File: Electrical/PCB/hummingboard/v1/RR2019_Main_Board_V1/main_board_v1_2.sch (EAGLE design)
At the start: 144 parts, among them CN1 MIRCO_B, IC1 OR_SC70-5, J10 I2C_5V_4, J11 SERVO_LEFT, J12 SERVO_RIGHT, J13 ESC, J14 5V_INPUT, J15 QUAD_ENCODER_2, J16 7.2V_INPUT, J17 I2C_5V_FXIO_1, J18 I2C_5V_FXIO_2, J19 JETSON_TRIGGER, J2 REAR_ENCODER, J20 QUAD_ENCODER_1, J21 BLDC_HALL, J22 SPI_FXIO_1, J3 FRONT_ENCODER, J4 I2C_1V8_1, J5 SPI_2, J6 WIRELESS_MODULE, J7 UART_0, J8 UART_2, J9 STEERING_ANGLE, Q1 BSS138, Q3 DMP2066LSN, Q4 BSS138, Q5 BSS138, Q6 BSS138, Q7 BSS138, Q8 BSS138, U3 ICM-20948, U4 PCA9306

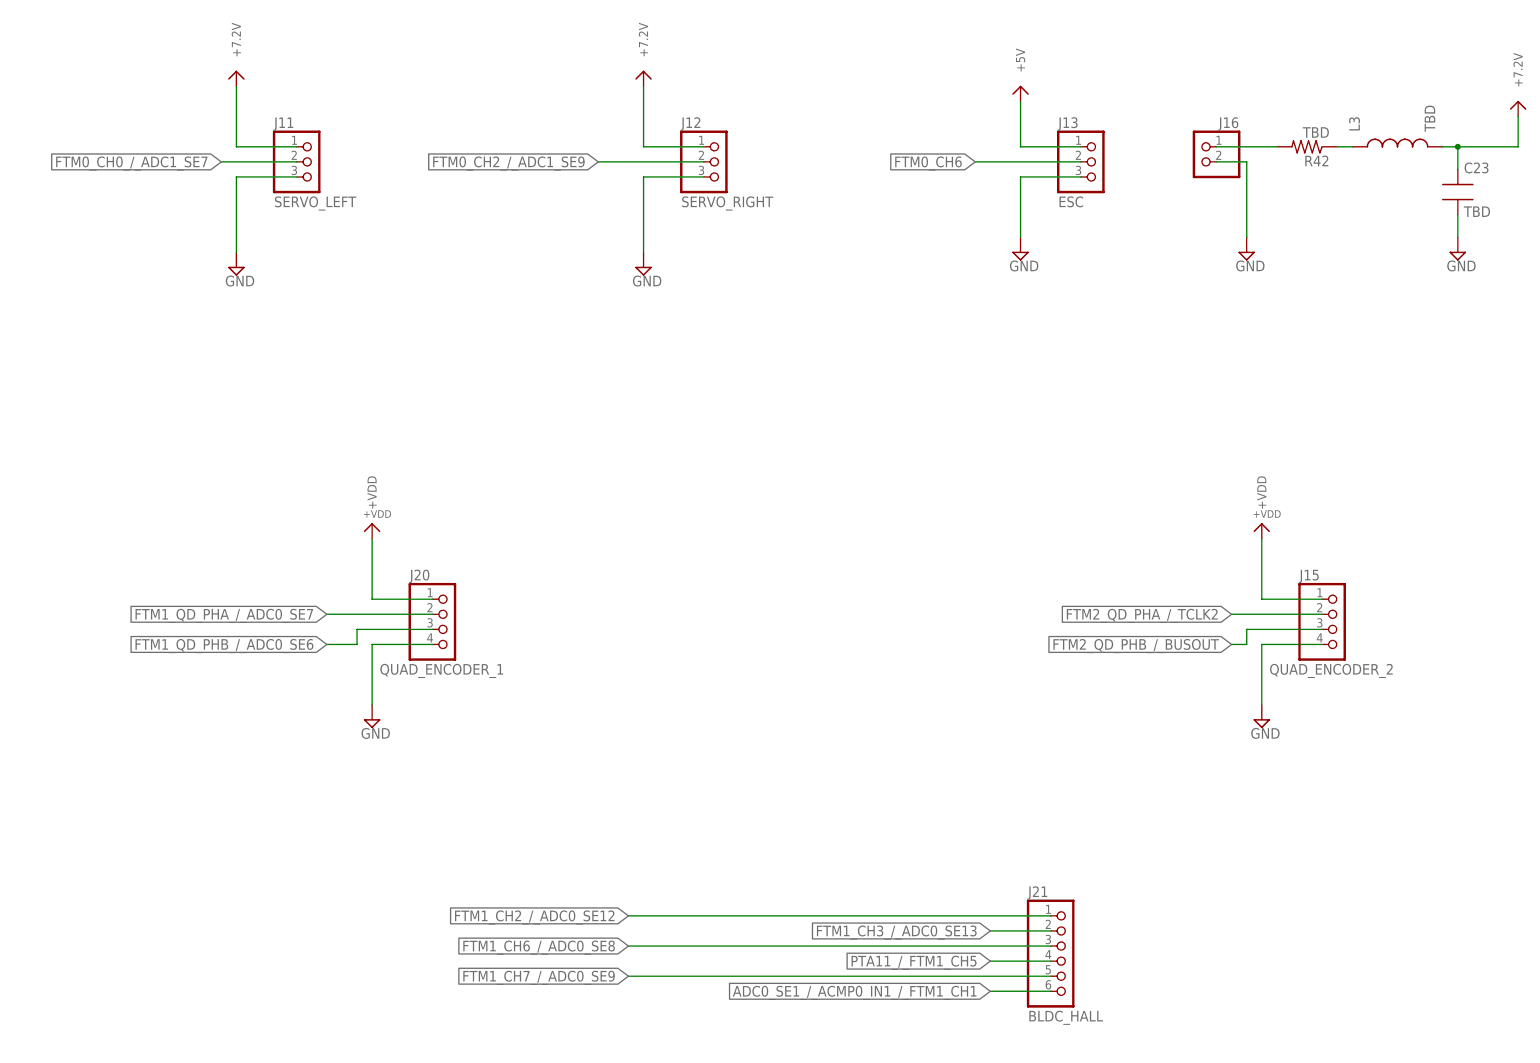
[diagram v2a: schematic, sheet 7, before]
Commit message: increase 7.2V power plane size
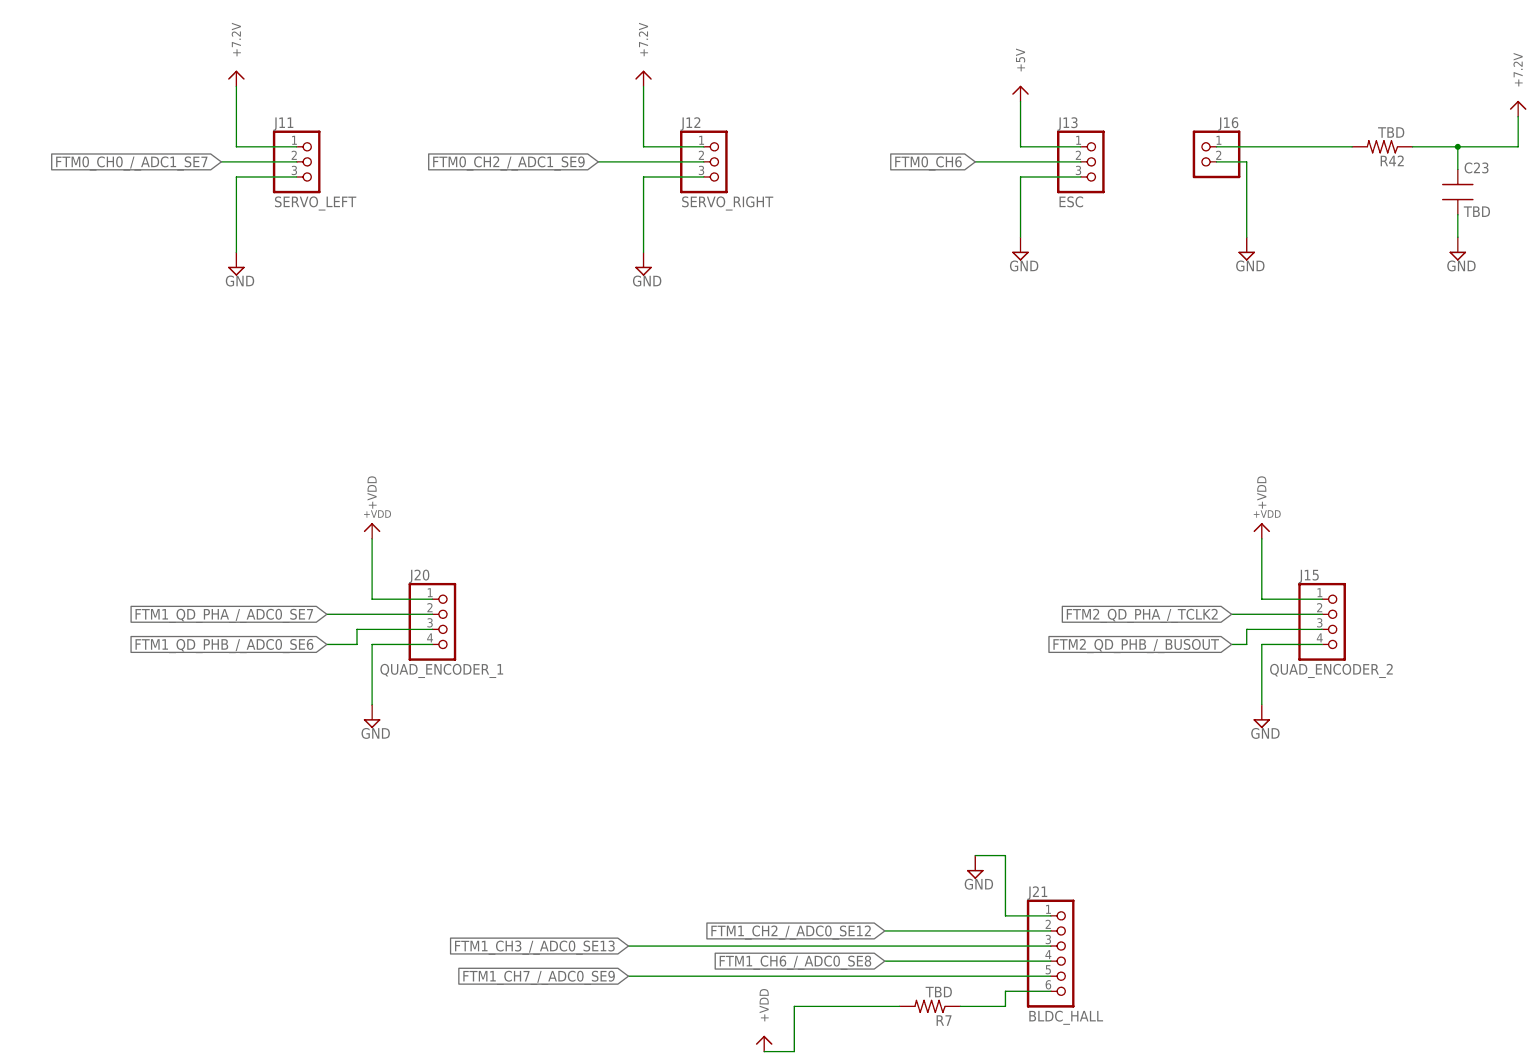
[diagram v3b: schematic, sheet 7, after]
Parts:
- removed L3: TBD, RobotRacing2019_Master:IND0603
- added R7: TBD, RobotRacing2019_Master:RES0603
- S3: value ON/OFF -> OFF/ON
- renumbered DEBUD/RACE to DEBUG/RACE
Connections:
- removed net N$36: L3.1, R42.1
- new net N$4: J21.6, R7.1
- net +7.2V: now also R42.1; no longer L3.2
- net +VDD: now also R7.2
- net ADC0_SE1_/_ACMP0_IN1_/_FTM1_CH1: no longer J21.6
- net FTM1_CH2_/_ADC0_SE12: now also J21.2; no longer J21.1
- net FTM1_CH3_/_ADC0_SE13: now also J21.3; no longer J21.2
- net FTM1_CH6_/_ADC0_SE8: now also J21.4; no longer J21.3
- net GND: now also J21.1
- net PTA11_/_FTM1_CH5: no longer J21.4
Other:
- moved on the sheet: R42
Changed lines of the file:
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@@
 <part name="J16" library="RobotRacing2019_Master" deviceset="PINHEAD-2-VERTICAL" device="" value="7.2V_INPUT"/>
 <part name="C23" library="RobotRacing2019_Master" deviceset="CAP0603" device="" value="TBD"/>
-<part name="L3" library="RobotRacing2019_Master" deviceset="IND0603" device="" value="TBD"/>
 <part name="R42" library="RobotRacing2019_Master" deviceset="RES0603" device="" value="TBD"/>
 <part name="SUPPLY42" library="RobotRacing2019_Master" deviceset="GND" device=""/>
@@
 <part name="U$29" library="RobotRacing2019_Master" deviceset="+1V8" device=""/>
 <part name="RC/AUTO" library="special" library_urn="urn:adsk.eagle:library:367" deviceset="SW_DIP-1" device="" package3d_urn="urn:adsk.eagle:package:26661/1"/>
-<part name="S3" library="RobotRacing2019_Master" deviceset="M9040P" device="" package3d_urn="urn:adsk.eagle:package:27676/1" value="ON/OFF"/>
-<part name="DEBUD/RACE" library="special" library_urn="urn:adsk.eagle:library:367" deviceset="SW_DIP-1" device="" package3d_urn="urn:adsk.eagle:package:26661/1"/>
+<part name="S3" library="RobotRacing2019_Master" deviceset="M9040P" device="" package3d_urn="urn:adsk.eagle:package:27676/1" value="OFF/ON"/>
+<part name="DEBUG/RACE" library="special" library_urn="urn:adsk.eagle:library:367" deviceset="SW_DIP-1" device="" package3d_urn="urn:adsk.eagle:package:26661/1"/>
 <part name="JP12" library="adafruit" library_urn="urn:adsk.eagle:library:420" deviceset="PINHD-1X3" device="" package3d_urn="urn:adsk.eagle:package:6240710/1" value="POWER2"/>
 <part name="SUPPLY16" library="RobotRacing2019_Master" deviceset="GND" device=""/>
 <part name="U$40" library="RobotRacing2019_Master" deviceset="+3V3" device=""/>
 <part name="U$44" library="RobotRacing2019_Master" deviceset="TEAM_LOGO" device=""/>
+<part name="R7" library="RobotRacing2019_Master" deviceset="RES0603" device="" value="TBD"/>
+<part name="U$47" library="RobotRacing2019_Master" deviceset="+VDD" device=""/>
+<part name="SUPPLY20" library="RobotRacing2019_Master" deviceset="GND" device=""/>
 </parts>
 <sheets>
@@
 <attribute name="VALUE" x="-312.42" y="16.51" size="1.778" layer="96" rot="R180"/>
 </instance>
-<instance part="DEBUD/RACE" gate="G$1" x="-271.78" y="-78.74" smashed="yes" rot="R270">
+<instance part="DEBUG/RACE" gate="G$1" x="-271.78" y="-78.74" smashed="yes" rot="R270">
 <attribute name="NAME" x="-268.605" y="-71.12" size="1.778" layer="95" rot="R270"/>
 <attribute name="VALUE" x="-276.86" y="-73.66" size="1.778" layer="96" rot="R270"/>
@@
 </segment>
 <segment>
-<pinref part="DEBUD/RACE" gate="G$1" pin="1"/>
+<pinref part="DEBUG/RACE" gate="G$1" pin="1"/>
 <pinref part="SUPPLY35" gate="GND" pin="GND"/>
 <wire x1="-271.78" y1="-86.36" x2="-271.78" y2="-91.44" width="0.1524" layer="91"/>
@@
 <segment>
 <pinref part="R15" gate="G$1" pin="1"/>
-<pinref part="DEBUD/RACE" gate="G$1" pin="2"/>
+<pinref part="DEBUG/RACE" gate="G$1" pin="2"/>
 <wire x1="-271.78" y1="-71.12" x2="-271.78" y2="-68.58" width="0.1524" layer="91"/>
 <pinref part="C22" gate="G$1" pin="1"/>
@@
 <attribute name="VALUE" x="120.396" y="11.049" size="1.778" layer="96"/>
 </instance>
-<instance part="L3" gate="G$1" x="109.22" y="22.86" smashed="yes" rot="R90">
-<attribute name="NAME" x="102.87" y="25.4" size="1.778" layer="95" rot="R90"/>
-<attribute name="VALUE" x="115.57" y="25.4" size="1.778" layer="96" rot="R90"/>
-</instance>
-<instance part="R42" gate="G$1" x="93.98" y="22.86" smashed="yes" rot="R180">
-<attribute name="NAME" x="97.79" y="21.3614" size="1.778" layer="95" rot="R180"/>
-<attribute name="VALUE" x="97.79" y="26.162" size="1.778" layer="96" rot="R180"/>
+<instance part="R42" gate="G$1" x="106.68" y="22.86" smashed="yes" rot="R180">
+<attribute name="NAME" x="110.49" y="21.3614" size="1.778" layer="95" rot="R180"/>
+<attribute name="VALUE" x="110.49" y="26.162" size="1.778" layer="96" rot="R180"/>
 </instance>
 <instance part="SUPPLY42" gate="GND" x="45.72" y="5.08" smashed="yes">
@@
 <instance part="U$32" gate="G$1" x="-17.78" y="33.02" smashed="yes"/>
 <instance part="U$63" gate="G$1" x="129.54" y="27.94" smashed="yes"/>
+<instance part="R7" gate="G$1" x="30.48" y="-121.92" smashed="yes" rot="R180">
+<attribute name="NAME" x="34.29" y="-123.4186" size="1.778" layer="95" rot="R180"/>
+<attribute name="VALUE" x="34.29" y="-118.618" size="1.778" layer="96" rot="R180"/>
+</instance>
+<instance part="U$47" gate="G$1" x="2.54" y="-127" smashed="yes"/>
+<instance part="SUPPLY20" gate="GND" x="38.1" y="-99.06" smashed="yes">
+<attribute name="VALUE" x="36.195" y="-102.235" size="1.778" layer="96"/>
+</instance>
 </instances>
 <busses>
@@
 <wire x1="-86.36" y1="17.78" x2="-76.2" y2="17.78" width="0.1524" layer="91"/>
 </segment>
+<segment>
+<pinref part="J21" gate="G$1" pin="1"/>
+<wire x1="50.8" y1="-106.68" x2="43.18" y2="-106.68" width="0.1524" layer="91"/>
+<wire x1="43.18" y1="-106.68" x2="43.18" y2="-96.52" width="0.1524" layer="91"/>
+<pinref part="SUPPLY20" gate="GND" pin="GND"/>
+<wire x1="38.1" y1="-96.52" x2="43.18" y2="-96.52" width="0.1524" layer="91"/>
+</segment>
 </net>
 <net name="FTM2_QD_PHA_/_TCLK2" class="0">
@@
 <net name="FTM1_CH2_/_ADC0_SE12" class="0">
 <segment>
-<wire x1="50.8" y1="-106.68" x2="-20.32" y2="-106.68" width="0.1524" layer="91"/>
-<label x="-20.32" y="-106.68" size="1.778" layer="95" rot="R180" xref="yes"/>
-<pinref part="J21" gate="G$1" pin="1"/>
+<label x="22.86" y="-109.22" size="1.778" layer="95" rot="R180" xref="yes"/>
+<pinref part="J21" gate="G$1" pin="2"/>
+<wire x1="50.8" y1="-109.22" x2="22.86" y2="-109.22" width="0.1524" layer="91"/>
 </segment>
 </net>
 <net name="FTM1_CH3_/_ADC0_SE13" class="0">
 <segment>
-<wire x1="50.8" y1="-109.22" x2="40.64" y2="-109.22" width="0.1524" layer="91"/>
-<label x="40.64" y="-109.22" size="1.778" layer="95" rot="R180" xref="yes"/>
-<pinref part="J21" gate="G$1" pin="2"/>
+<label x="-20.32" y="-111.76" size="1.778" layer="95" rot="R180" xref="yes"/>
+<pinref part="J21" gate="G$1" pin="3"/>
+<wire x1="50.8" y1="-111.76" x2="-20.32" y2="-111.76" width="0.1524" layer="91"/>
 </segment>
 </net>
@@
 <net name="FTM1_CH6_/_ADC0_SE8" class="0">
 <segment>
-<label x="-20.32" y="-111.76" size="1.778" layer="95" rot="R180" xref="yes"/>
-<pinref part="J21" gate="G$1" pin="3"/>
-<wire x1="-20.32" y1="-111.76" x2="50.8" y2="-111.76" width="0.1524" layer="91"/>
+<label x="22.86" y="-114.3" size="1.778" layer="95" rot="R180" xref="yes"/>
+<pinref part="J21" gate="G$1" pin="4"/>
+<wire x1="50.8" y1="-114.3" x2="22.86" y2="-114.3" width="0.1524" layer="91"/>
 </segment>
 </net>
@@
 </segment>
 </net>
-<net name="PTA11_/_FTM1_CH5" class="0">
-<segment>
-<pinref part="J21" gate="G$1" pin="4"/>
-<wire x1="50.8" y1="-114.3" x2="40.64" y2="-114.3" width="0.1524" layer="91"/>
-<label x="40.64" y="-114.3" size="1.778" layer="95" rot="R180" xref="yes"/>
-</segment>
-</net>
-<net name="ADC0_SE1_/_ACMP0_IN1_/_FTM1_CH1" class="0">
-<segment>
-<pinref part="J21" gate="G$1" pin="6"/>
-<wire x1="50.8" y1="-119.38" x2="40.64" y2="-119.38" width="0.1524" layer="91"/>
-<label x="40.64" y="-119.38" size="1.778" layer="95" rot="R180" xref="yes"/>
-</segment>
-</net>
 <net name="+7.2V" class="0">
 <segment>
@@
 <wire x1="119.38" y1="22.86" x2="129.54" y2="22.86" width="0.1524" layer="91"/>
 <wire x1="119.38" y1="19.05" x2="119.38" y2="22.86" width="0.1524" layer="91"/>
-<pinref part="L3" gate="G$1" pin="2"/>
-<wire x1="116.84" y1="22.86" x2="119.38" y2="22.86" width="0.1524" layer="91"/>
 <junction x="119.38" y="22.86"/>
 <pinref part="U$63" gate="G$1" pin="+7.2V"/>
 <wire x1="129.54" y1="22.86" x2="129.54" y2="27.94" width="0.1524" layer="91"/>
+<pinref part="R42" gate="G$1" pin="1"/>
+<wire x1="111.76" y1="22.86" x2="119.38" y2="22.86" width="0.1524" layer="91"/>
 </segment>
 <segment>
@@
 <segment>
 <pinref part="J16" gate="G$1" pin="1"/>
-<wire x1="78.74" y1="22.86" x2="88.9" y2="22.86" width="0.1524" layer="91"/>
+<wire x1="78.74" y1="22.86" x2="101.6" y2="22.86" width="0.1524" layer="91"/>
 <pinref part="R42" gate="G$1" pin="2"/>
 </segment>
 </net>
-<net name="N$36" class="0">
-<segment>
-<pinref part="L3" gate="G$1" pin="1"/>
-<wire x1="101.6" y1="22.86" x2="99.06" y2="22.86" width="0.1524" layer="91"/>
-<pinref part="R42" gate="G$1" pin="1"/>
-</segment>
-</net>
 <net name="+VDD" class="0">
 <segment>
@@
 <pinref part="U$39" gate="G$1" pin="+VDD"/>
 </segment>
+<segment>
+<pinref part="R7" gate="G$1" pin="2"/>
+<wire x1="7.62" y1="-121.92" x2="25.4" y2="-121.92" width="0.1524" layer="91"/>
+<wire x1="7.62" y1="-121.92" x2="7.62" y2="-129.54" width="0.1524" layer="91"/>
+<pinref part="U$47" gate="G$1" pin="+VDD"/>
+<wire x1="2.54" y1="-129.54" x2="7.62" y2="-129.54" width="0.1524" layer="91"/>
+</segment>
+</net>
+<net name="N$4" class="0">
+<segment>
+<pinref part="R7" gate="G$1" pin="1"/>
+<wire x1="35.56" y1="-121.92" x2="43.18" y2="-121.92" width="0.1524" layer="91"/>
+<wire x1="43.18" y1="-121.92" x2="43.18" y2="-119.38" width="0.1524" layer="91"/>
+<pinref part="J21" gate="G$1" pin="6"/>
+<wire x1="43.18" y1="-119.38" x2="50.8" y2="-119.38" width="0.1524" layer="91"/>
+</segment>
 </net>

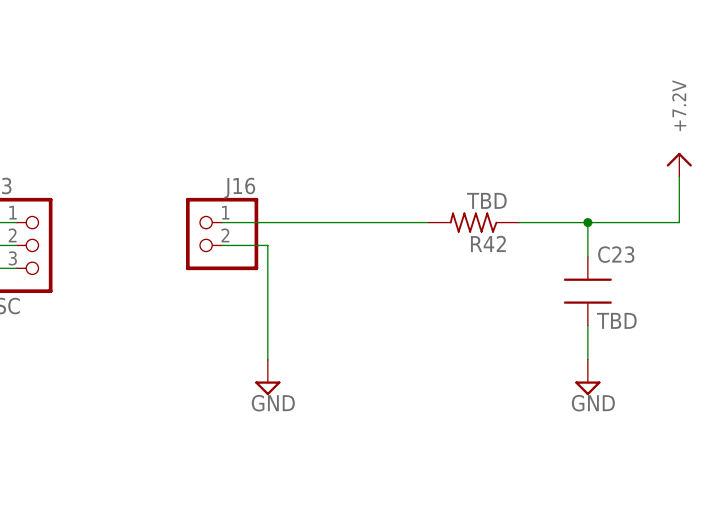
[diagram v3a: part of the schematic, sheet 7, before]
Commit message: remove inductor from 7.2V input / modify GND plane
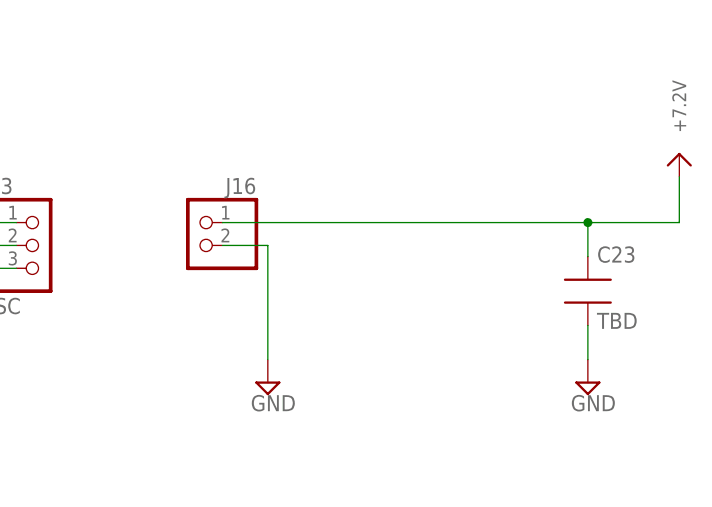
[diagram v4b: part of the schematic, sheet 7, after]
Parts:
- removed R42: TBD, RobotRacing2019_Master:RES0603
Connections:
- removed net N$34: J16.1, R42.2
- net +7.2V: now also J16.1; no longer R42.1
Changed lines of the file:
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@@
 <part name="J16" library="RobotRacing2019_Master" deviceset="PINHEAD-2-VERTICAL" device="" value="7.2V_INPUT"/>
 <part name="C23" library="RobotRacing2019_Master" deviceset="CAP0603" device="" value="TBD"/>
-<part name="R42" library="RobotRacing2019_Master" deviceset="RES0603" device="" value="TBD"/>
 <part name="SUPPLY42" library="RobotRacing2019_Master" deviceset="GND" device=""/>
 <part name="SUPPLY40" library="RobotRacing2019_Master" deviceset="GND" device=""/>
@@
 <attribute name="VALUE" x="120.396" y="11.049" size="1.778" layer="96"/>
 </instance>
-<instance part="R42" gate="G$1" x="106.68" y="22.86" smashed="yes" rot="R180">
-<attribute name="NAME" x="110.49" y="21.3614" size="1.778" layer="95" rot="R180"/>
-<attribute name="VALUE" x="110.49" y="26.162" size="1.778" layer="96" rot="R180"/>
-</instance>
 <instance part="SUPPLY42" gate="GND" x="45.72" y="5.08" smashed="yes">
 <attribute name="VALUE" x="43.815" y="1.905" size="1.778" layer="96"/>
@@
 <pinref part="U$63" gate="G$1" pin="+7.2V"/>
 <wire x1="129.54" y1="22.86" x2="129.54" y2="27.94" width="0.1524" layer="91"/>
-<pinref part="R42" gate="G$1" pin="1"/>
-<wire x1="111.76" y1="22.86" x2="119.38" y2="22.86" width="0.1524" layer="91"/>
+<pinref part="J16" gate="G$1" pin="1"/>
+<wire x1="78.74" y1="22.86" x2="119.38" y2="22.86" width="0.1524" layer="91"/>
 </segment>
 <segment>
@@
 </segment>
 </net>
-<net name="N$34" class="0">
-<segment>
-<pinref part="J16" gate="G$1" pin="1"/>
-<wire x1="78.74" y1="22.86" x2="101.6" y2="22.86" width="0.1524" layer="91"/>
-<pinref part="R42" gate="G$1" pin="2"/>
-</segment>
-</net>
